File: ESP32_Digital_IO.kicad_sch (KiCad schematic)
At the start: 23 parts, among them J2 217179-0001, J3 DIGITAL_IO_3V3, U3 ESP32-S3-WROOM-1-N16R8

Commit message: added remaining pages. BOM and refinement is all thats left
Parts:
- removed D2, D3: SP0504BAHT, Package_TO_SOT_SMD:SOT-23-5, symbol Power_Protection:SP0504BAHT
- added D2: TLHR-6400, LED_SMD:LED_Cree-XHP50_3V_HighDensity, symbol Device:LED
- added D3: TLHY-6400, LED_SMD:LED_Cree-XHP50_3V_HighDensity, symbol Device:LED
- added R2, R34: LED_R_TBD, symbol Device:R
- added U4, U5: D3V3XA4B10LP, Package_DFN_QFN:Diodes_UDFN-10_1x2.5mm_P0.5mm, symbol Power_Protection:D3V3XA4B10LP
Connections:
- net +3.3V: now also R2.1
- net GND: now also D2.1 (K), D3.1 (K), U4.3 (VSS), U4.8 (VSS), U5.3 (VSS), U5.8 (VSS)
- net USB_VBUS_SENSE: now reaches R7.1, R8.2
- net USB_VBUS_SENSE: now also U3.38 (IO2); no longer U3.23 (IO21)
- net at J3.8 (Pin_8), R16.1: now also U5.5
- net at J3.7 (Pin_7), R15.1: now also U5.4
- net at J3.1 (Pin_1), R9.1: now also U4.1
- net at J3.2 (Pin_2), R10.1: now also U4.2
- net at J3.3 (Pin_3), R11.1: now also U4.5
- net at J3.4 (Pin_4), R12.1: now also U4.4
- net at J3.5 (Pin_5), R13.1: now also U5.2
- net at J3.6 (Pin_6), R14.1: now also U5.1
- net TC_CS: now reaches U3.10 (IO17)
- net ADC1_DRDY: now reaches U3.11 (IO18)
- net SPI_SCK: now reaches U3.20 (IO12)
- net SPI_PICO: now reaches U3.21 (IO13)
- net SPI_POCI: now reaches U3.22 (IO14)
- net ADC2_PWDN: now reaches U3.24 (IO47)
- net TC_DRDY: now reaches U3.25 (IO48)
- net ADC1_START: now reaches U3.31 (IO38)
- net ADC2_START: now reaches U3.32 (IO39)
- net ADC1_RESET: now reaches U3.33 (IO40)
- net ADC2_RESET: now reaches U3.34 (IO41)
- net ADC1_PWDN: now reaches U3.35 (IO42)
- net WIFI_LED: now reaches U3.37 (TXD0)
- net WIFI_LED: now also R34.1
- net TC_FAULT: now reaches U3.39 (IO1)
- net ADC1_CS: now reaches U3.8 (IO15)
- net ADC2_CS: now reaches U3.9 (IO16)
- new net: D3.2 (A), R34.2
- new net: D2.2 (A), R2.2
- new net ADC2_DRDY: U3.23 (IO21)
- no-connect marks 2 -> 10
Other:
- moved on the sheet: C4, C5, D1, J2, J3, R1, R10, R11, R12, R13, R14, R15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

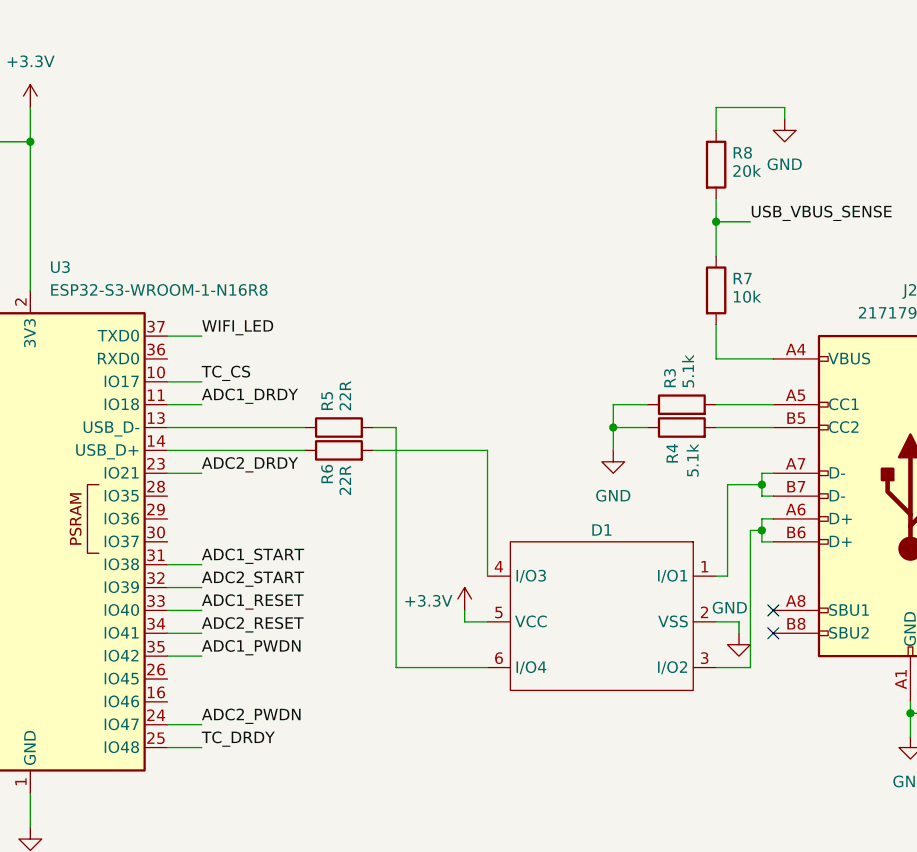
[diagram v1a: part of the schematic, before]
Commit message: Added a few comments in blue text
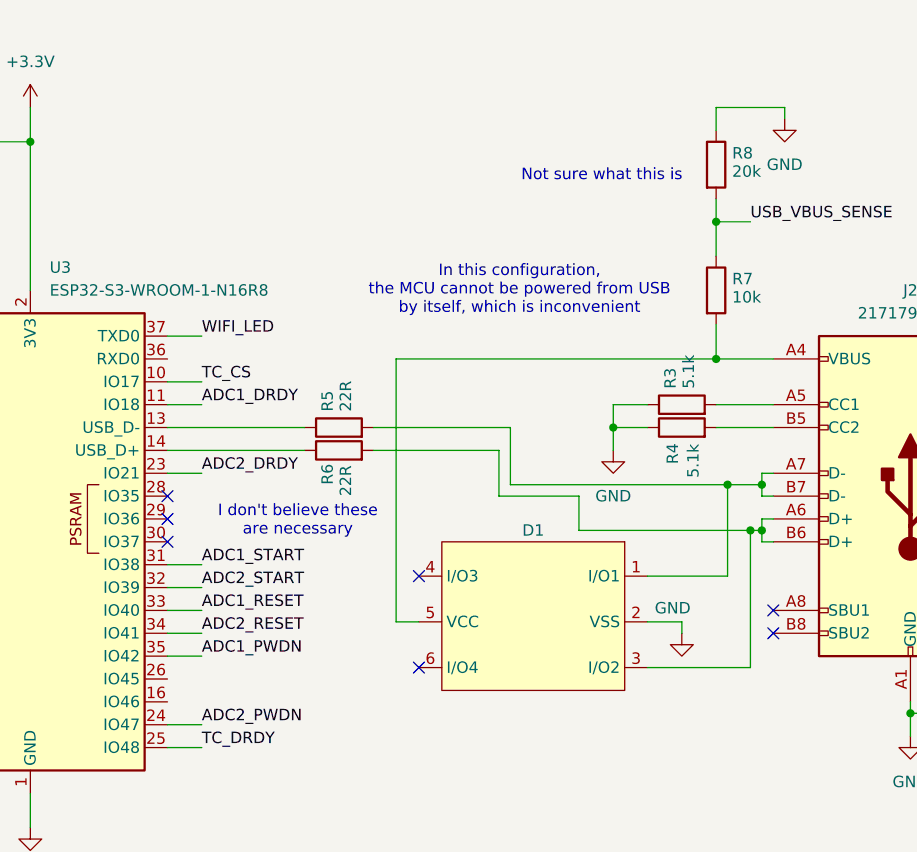
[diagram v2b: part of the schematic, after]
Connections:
- net +3.3V: no longer D1.5 (VCC)
- net at J2.A4 (VBUS), J2.A9 (VBUS), J2.B4 (VBUS)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: now also D1.5 (VCC)
- net at R6.2: now also D1.3 (I/O2), J2.A6 (D+), J2.B6 (D+); no longer D1.4 (I/O3)
- net at R5.2: now also D1.1 (I/O1), J2.A7 (D-), J2.B7 (D-); no longer D1.6 (I/O4)
- no-connect marks 10 -> 15
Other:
- note added: "I don't believe these are necessary"
- note added: "In this configuration, the MCU cannot be powered from USB by itself, which is inconvenient"
- note added: "Not sure what this is"

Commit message: finished schematic draft 1
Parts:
- D1: value (none) -> DT1042-04SO-7; MPN (none) -> DT1042-04SO-7; Manufacturer (none) -> Diodes Incorporated
- D2: footprint LED_SMD:LED_Cree-XHP50_3V_HighDensity -> LED_THT:LED_D5.0mm; MPN (none) -> TLHR6400; Manufacturer (none) -> Vishay
- D3: footprint LED_SMD:LED_Cree-XHP50_3V_HighDensity -> LED_THT:LED_D5.0mm; MPN (none) -> TLHY6400; Manufacturer (none) -> Vishay
- J2: footprint (none) -> Connector_USB:USB_C_Plug_JAE_DX07P024AJ1; MPN (none) -> 217179-0001; Manufacturer (none) -> Molex
- J3: footprint (none) -> TerminalBlock_Phoenix:TerminalBlock_Phoenix_MKDS-1,5-8-5.08_1x08_P5.08mm_Horizontal; MPN (none) -> 1729128; Manufacturer (none) -> Phoenix Contact
- R2, R34: value LED_R_TBD -> 330R
- U3: value ESP32-S3-WROOM-1-N16R8 -> ESP32-S3; MPN (none) -> ESP32-S3-WROOM-1-N16R8; Manufacturer (none) -> Espressif Systems
- U4, U5: MPN (none) -> D3V3XA4B10LP-7; Manufacturer (none) -> Diodes Incorporated
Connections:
- net +3.3V: now also D1.5 (VCC), J2.A4 (VBUS), J2.A9 (VBUS), J2.B4 (VBUS), J2.B9 (VBUS), R7.2
- no-connect marks 15 -> 20
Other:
- note removed: "I don't believe these are necessary"
- note removed: "In this configuration, the MCU cannot be powered from USB by itself, which is inconvenient"
- note removed: "Not sure what this is"
- moved on the sheet: C5, R1

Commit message: Fixed some issues and renamed project
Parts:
- D1: symbol Custom_DT1042-04SO-7:DT1042-04SO-7 -> Custom_Symbols:DT1042-04SO-7
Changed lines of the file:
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@@
 		)
 		(instances
-			(project "capstoneKicad"
+			(project "slapdaq-board"
 				(path "/13b31ec5-9d44-45c3-b3e5-a18c48e5f516/f3b0adef-1da3-4963-a2de-79e7f8ea7f57"
 					(reference "#PWR043")
@@
 		)
 		(instances
-			(project "capstoneKicad"
+			(project "slapdaq-board"
 				(path "/13b31ec5-9d44-45c3-b3e5-a18c48e5f516/f3b0adef-1da3-4963-a2de-79e7f8ea7f57"
 					(reference "R34")
@@
 		)
 		(instances
-			(project "capstoneKicad"
+			(project "slapdaq-board"
 				(path "/13b31ec5-9d44-45c3-b3e5-a18c48e5f516/f3b0adef-1da3-4963-a2de-79e7f8ea7f57"
 					(reference "R7")
@@
 		)
 		(instances
-			(project "capstoneKicad"
+			(project "slapdaq-board"
 				(path "/13b31ec5-9d44-45c3-b3e5-a18c48e5f516/f3b0adef-1da3-4963-a2de-79e7f8ea7f57"
 					(reference "#PWR012")
@@
 		)
 		(instances
-			(project "capstoneKicad"
+			(project "slapdaq-board"
 				(path "/13b31ec5-9d44-45c3-b3e5-a18c48e5f516/f3b0adef-1da3-4963-a2de-79e7f8ea7f57"
 					(reference "R6")
@@
 		)
 		(instances
-			(project "capstoneKicad"
+			(project "slapdaq-board"
 				(path "/13b31ec5-9d44-45c3-b3e5-a18c48e5f516/f3b0adef-1da3-4963-a2de-79e7f8ea7f57"
 					(reference "U5")
@@
 		)
 		(instances
-			(project "capstoneKicad"
+			(project "slapdaq-board"
 				(path "/13b31ec5-9d44-45c3-b3e5-a18c48e5f516/f3b0adef-1da3-4963-a2de-79e7f8ea7f57"
 					(reference "R16")
@@
 		)
 		(instances
-			(project "capstoneKicad"
+			(project "slapdaq-board"
 				(path "/13b31ec5-9d44-45c3-b3e5-a18c48e5f516/f3b0adef-1da3-4963-a2de-79e7f8ea7f57"
 					(reference "R5")
@@
 		)
 		(instances
-			(project "capstoneKicad"
+			(project "slapdaq-board"
 				(path "/13b31ec5-9d44-45c3-b3e5-a18c48e5f516/f3b0adef-1da3-4963-a2de-79e7f8ea7f57"
 					(reference "#PWR08")
@@
 		)
 		(instances
-			(project "capstoneKicad"
+			(project "slapdaq-board"
 				(path "/13b31ec5-9d44-45c3-b3e5-a18c48e5f516/f3b0adef-1da3-4963-a2de-79e7f8ea7f57"
 					(reference "R15")
@@
 		)
 		(instances
-			(project "capstoneKicad"
+			(project "slapdaq-board"
 				(path "/13b31ec5-9d44-45c3-b3e5-a18c48e5f516/f3b0adef-1da3-4963-a2de-79e7f8ea7f57"
 					(reference "#PWR017")
@@
 		)
 		(instances
-			(project "capstoneKicad"
+			(project "slapdaq-board"
 				(path "/13b31ec5-9d44-45c3-b3e5-a18c48e5f516/f3b0adef-1da3-4963-a2de-79e7f8ea7f57"
 					(reference "#PWR062")
@@
 	)
 	(symbol
-		(lib_id "Custom_DT1042-04SO-7:DT1042-04SO-7")
+		(lib_id "Custom_Symbols:DT1042-04SO-7")
 		(at 191.77 111.76 0)
 		(mirror y)
@@
 		)
 		(instances
-			(project "capstoneKicad"
+			(project "slapdaq-board"
 				(path "/13b31ec5-9d44-45c3-b3e5-a18c48e5f516/f3b0adef-1da3-4963-a2de-79e7f8ea7f57"
 					(reference "D1")
@@
 		)
 		(instances
-			(project "capstoneKicad"
+			(project "slapdaq-board"
 				(path "/13b31ec5-9d44-45c3-b3e5-a18c48e5f516/f3b0adef-1da3-4963-a2de-79e7f8ea7f57"
 					(reference "#PWR016")
@@
 		)
 		(instances
-			(project "capstoneKicad"
+			(project "slapdaq-board"
 				(path "/13b31ec5-9d44-45c3-b3e5-a18c48e5f516/f3b0adef-1da3-4963-a2de-79e7f8ea7f57"
 					(reference "#PWR021")
@@
 		)
 		(instances
-			(project "capstoneKicad"
+			(project "slapdaq-board"
 				(path "/13b31ec5-9d44-45c3-b3e5-a18c48e5f516/f3b0adef-1da3-4963-a2de-79e7f8ea7f57"
 					(reference "R13")
@@
 		)
 		(instances
-			(project "capstoneKicad"
+			(project "slapdaq-board"
 				(path "/13b31ec5-9d44-45c3-b3e5-a18c48e5f516/f3b0adef-1da3-4963-a2de-79e7f8ea7f57"
 					(reference "U4")
@@
 		)
 		(instances
-			(project "capstoneKicad"
+			(project "slapdaq-board"
 				(path "/13b31ec5-9d44-45c3-b3e5-a18c48e5f516/f3b0adef-1da3-4963-a2de-79e7f8ea7f57"
 					(reference "#PWR011")
@@
 		)
 		(instances
-			(project "capstoneKicad"
+			(project "slapdaq-board"
 				(path "/13b31ec5-9d44-45c3-b3e5-a18c48e5f516/f3b0adef-1da3-4963-a2de-79e7f8ea7f57"
 					(reference "#PWR019")
@@
 		)
 		(instances
-			(project "capstoneKicad"
+			(project "slapdaq-board"
 				(path "/13b31ec5-9d44-45c3-b3e5-a18c48e5f516/f3b0adef-1da3-4963-a2de-79e7f8ea7f57"
 					(reference "#PWR020")
@@
 		)
 		(instances
-			(project "capstoneKicad"
+			(project "slapdaq-board"
 				(path "/13b31ec5-9d44-45c3-b3e5-a18c48e5f516/f3b0adef-1da3-4963-a2de-79e7f8ea7f57"
 					(reference "#PWR010")
@@
 		)
 		(instances
-			(project "capstoneKicad"
+			(project "slapdaq-board"
 				(path "/13b31ec5-9d44-45c3-b3e5-a18c48e5f516/f3b0adef-1da3-4963-a2de-79e7f8ea7f57"
 					(reference "C4")
@@
 		)
 		(instances
-			(project "capstoneKicad"
+			(project "slapdaq-board"
 				(path "/13b31ec5-9d44-45c3-b3e5-a18c48e5f516/f3b0adef-1da3-4963-a2de-79e7f8ea7f57"
 					(reference "D2")
@@
 		)
 		(instances
-			(project "capstoneKicad"
+			(project "slapdaq-board"
 				(path "/13b31ec5-9d44-45c3-b3e5-a18c48e5f516/f3b0adef-1da3-4963-a2de-79e7f8ea7f57"
 					(reference "R2")
@@
 		)
 		(instances
-			(project "capstoneKicad"
+			(project "slapdaq-board"
 				(path "/13b31ec5-9d44-45c3-b3e5-a18c48e5f516/f3b0adef-1da3-4963-a2de-79e7f8ea7f57"
 					(reference "#PWR060")
@@
 		)
 		(instances
-			(project "capstoneKicad"
+			(project "slapdaq-board"
 				(path "/13b31ec5-9d44-45c3-b3e5-a18c48e5f516/f3b0adef-1da3-4963-a2de-79e7f8ea7f57"
 					(reference "R12")
@@
 		)
 		(instances
-			(project "capstoneKicad"
+			(project "slapdaq-board"
 				(path "/13b31ec5-9d44-45c3-b3e5-a18c48e5f516/f3b0adef-1da3-4963-a2de-79e7f8ea7f57"
 					(reference "R1")
@@
 		)
 		(instances
-			(project "capstoneKicad"
+			(project "slapdaq-board"
 				(path "/13b31ec5-9d44-45c3-b3e5-a18c48e5f516/f3b0adef-1da3-4963-a2de-79e7f8ea7f57"
 					(reference "R14")
@@
 		)
 		(instances
-			(project "capstoneKicad"
+			(project "slapdaq-board"
 				(path "/13b31ec5-9d44-45c3-b3e5-a18c48e5f516/f3b0adef-1da3-4963-a2de-79e7f8ea7f57"
 					(reference "#PWR09")
@@
 		)
 		(instances
-			(project "capstoneKicad"
+			(project "slapdaq-board"
 				(path "/13b31ec5-9d44-45c3-b3e5-a18c48e5f516/f3b0adef-1da3-4963-a2de-79e7f8ea7f57"
 					(reference "R3")
@@
 		)
 		(instances
-			(project "capstoneKicad"
+			(project "slapdaq-board"
 				(path "/13b31ec5-9d44-45c3-b3e5-a18c48e5f516/f3b0adef-1da3-4963-a2de-79e7f8ea7f57"
 					(reference "#PWR015")
@@
 		)
 		(instances
-			(project "capstoneKicad"
+			(project "slapdaq-board"
 				(path "/13b31ec5-9d44-45c3-b3e5-a18c48e5f516/f3b0adef-1da3-4963-a2de-79e7f8ea7f57"
 					(reference "#PWR059")
@@
 		)
 		(instances
-			(project "capstoneKicad"
+			(project "slapdaq-board"
 				(path "/13b31ec5-9d44-45c3-b3e5-a18c48e5f516/f3b0adef-1da3-4963-a2de-79e7f8ea7f57"
 					(reference "R10")
@@
 		)
 		(instances
-			(project "capstoneKicad"
+			(project "slapdaq-board"
 				(path "/13b31ec5-9d44-45c3-b3e5-a18c48e5f516/f3b0adef-1da3-4963-a2de-79e7f8ea7f57"
 					(reference "J3")
@@
 		)
 		(instances
-			(project "capstoneKicad"
+			(project "slapdaq-board"
 				(path "/13b31ec5-9d44-45c3-b3e5-a18c48e5f516/f3b0adef-1da3-4963-a2de-79e7f8ea7f57"
 					(reference "D3")
@@
 		)
 		(instances
-			(project "capstoneKicad"
+			(project "slapdaq-board"
 				(path "/13b31ec5-9d44-45c3-b3e5-a18c48e5f516/f3b0adef-1da3-4963-a2de-79e7f8ea7f57"
 					(reference "R8")
@@
 		)
 		(instances
-			(project "capstoneKicad"
+			(project "slapdaq-board"
 				(path "/13b31ec5-9d44-45c3-b3e5-a18c48e5f516/f3b0adef-1da3-4963-a2de-79e7f8ea7f57"
 					(reference "C5")
@@
 		)
 		(instances
-			(project "capstoneKicad"
+			(project "slapdaq-board"
 				(path "/13b31ec5-9d44-45c3-b3e5-a18c48e5f516/f3b0adef-1da3-4963-a2de-79e7f8ea7f57"
 					(reference "U3")
@@
 		)
 		(instances
-			(project "capstoneKicad"
+			(project "slapdaq-board"
 				(path "/13b31ec5-9d44-45c3-b3e5-a18c48e5f516/f3b0adef-1da3-4963-a2de-79e7f8ea7f57"
 					(reference "R11")
@@
 		)
 		(instances
-			(project "capstoneKicad"
+			(project "slapdaq-board"
 				(path "/13b31ec5-9d44-45c3-b3e5-a18c48e5f516/f3b0adef-1da3-4963-a2de-79e7f8ea7f57"
 					(reference "R9")
@@
 		)
 		(instances
-			(project "capstoneKicad"
+			(project "slapdaq-board"
 				(path "/13b31ec5-9d44-45c3-b3e5-a18c48e5f516/f3b0adef-1da3-4963-a2de-79e7f8ea7f57"
 					(reference "R4")
@@
 		)
 		(instances
-			(project "capstoneKicad"
+			(project "slapdaq-board"
 				(path "/13b31ec5-9d44-45c3-b3e5-a18c48e5f516/f3b0adef-1da3-4963-a2de-79e7f8ea7f57"
 					(reference "J2")

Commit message: "combined analog voltage and differential voltage sheets
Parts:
- added J10, J11, J5, J9: Conn_01x02, symbol Connector_Generic:Conn_01x02
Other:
- moved on the sheet: U5

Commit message: Grayson changes 9/11/26
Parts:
- removed R10, R11, R12, R13, R14, R15, R16, R9: 100R, symbol Device:R
- J2: MPN 217179-0001 -> USB4110-GF-A; Manufacturer Molex -> GCT
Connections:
- net at J3.6 (Pin_6), U5.1: now also U3.17 (IO9)
- net at J3.5 (Pin_5), U5.2: now also U3.12 (IO8)
- net at J3.7 (Pin_7), U5.4: now also U3.18 (IO10)
- net at J3.8 (Pin_8), U5.5: now also U3.19 (IO11)
- net at J3.1 (Pin_1), U4.1: now also U3.4 (IO4)
- net at J3.2 (Pin_2), U4.2: now also U3.5 (IO5)
- net at J3.4 (Pin_4), U4.4: now also U3.7 (IO7)
- net at J3.3 (Pin_3), U4.5: now also U3.6 (IO6)
- net TC_DRDY: no longer names the net of U3.25 (IO48)
- net TC_FAULT: no longer names the net of U3.39 (IO1)
- no-connect marks 20 -> 22
